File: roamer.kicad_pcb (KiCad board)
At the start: 4 copper layers, 39 x 99 mm, 97 parts, among them J1 Conn_Coaxial_Small, J2 JSTPH, J3 Conn_02x05_Odd_Even, J4 Conn_Coaxial_Small, J6 Conn_02x05_Odd_Even, J8 MEM2075-00-140-01-A, Q3 DMP2070UQ-7, SW1 KMR2, U1 2MB Flash, U2 AP2112K-3.3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

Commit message: Added mounting holes
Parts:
- removed JP2: SolderJumper_2_Open, Jumper:SolderJumper-2_P1.3mm_Open_TrianglePad1.0x1.5mm
- removed R29: 10K, Resistor_SMD:R_0603_1608Metric
- added C19: 1uF, Capacitor_SMD:C_0603_1608Metric, F.Cu at (243.8, 160.2)
- added H1: MountingHole, MountingHole:MountingHole_2.2mm_M2_DIN965_Pad, F.Cu at (220.5, 85.5)
- added H2: MountingHole, MountingHole:MountingHole_2.2mm_M2_DIN965_Pad, F.Cu at (220.2, 179.2)
- added H3: MountingHole, MountingHole:MountingHole_2.2mm_M2_DIN965_Pad, F.Cu at (253.8, 179.2)
- added H4: MountingHole, MountingHole:MountingHole_2.2mm_M2_DIN965_Pad, F.Cu at (253.5, 85.5)
- added H5: MountingHole, MountingHole:MountingHole_2.2mm_M2_DIN965_Pad, F.Cu at (220.5, 115.5)
- added R46: 0, Resistor_SMD:R_0603_1608Metric, F.Cu at (218.8, 134.5)
- added R47: 0, Resistor_SMD:R_0603_1608Metric, F.Cu at (218.8, 128.2)
- C10: value 10uF -> 1uF; footprint Inductor_SMD:L_0805_2012Metric -> Capacitor_SMD:C_0603_1608Metric
- moved TP8 4.32 mm to (253.6, 174.6)
- moved TP9 3.42 mm to (253.6, 170.5)
- moved J6 1.69 mm to (226.4, 177.4)
- moved R9 0.17 mm to (221.2, 167.5)
- moved C10 0.08 mm to (243.8, 152.2), turned to 90 degrees
- moved U1 0.08 mm to (240.0, 152.2)
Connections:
- C10 pad 1: +3V3 -> GND
- C10 pad 2: GND -> +3V3
- J2 pad 1: GND -> +BATT
- J2 pad 2: +BATT -> GND
- MCU1 pad 39: unconnected-(MCU1-PB16-Pad39) -> /Comms - LoRa 900/LORA_900_BUSY
- MCU1 pad 40: unconnected-(MCU1-PB17-Pad40) -> /Comms - LoRa 433/LORA_433_BUSY
- U4 pad 14: unconnected-(U4-DIO0-Pad14) -> Net-(U4-DIO0)
- U7 pad 5: Net-(JP2-B) -> unconnected-(U7-SDO-Pad5)
- U9 pad 14: unconnected-(U9-DIO0-Pad14) -> Net-(U9-DIO0)
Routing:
- net Net-(U4-DIO0): track 0.00 -> 36.2 mm, vias 0 -> 2
- net /Comms - LoRa 900/LORA_900_BUSY: track 0.00 -> 24.8 mm, vias 0 -> 2
- net /Comms - LoRa 433/LORA_433_BUSY: track 0.00 -> 17.6 mm, vias 0 -> 2
- net Net-(U9-DIO0): track 0.00 -> 14.6 mm, vias 0 -> 2
- net Net-(JP2-B): track 5.57 -> 0.00 mm, vias 1 -> 0
- net /Power - Management/IN-: track 30.8 -> 27.2 mm
- net Net-(U8-VS): track 2.81 -> 6.06 mm
- net +BATT: track 88.7 -> 85.8 mm
- net VBUS: track 60.7 -> 58.1 mm
- net /Bus - SPI/SPI.SCK: track 54.0 -> 56.6 mm
- net /Bus - SPI/SPI.MOSI: track 62.4 -> 60.7 mm
- net Net-(J3-Pin_10): track 35.9 -> 34.6 mm
- net Net-(D2-K): track 52.4 -> 51.1 mm
- net /Bus - SPI/SPI.MISO: track 69.4 -> 70.6 mm
- net +3V3: track 71.5 -> 72.7 mm, vias 16 -> 18
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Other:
- outline, holes or cut-outs redrawn

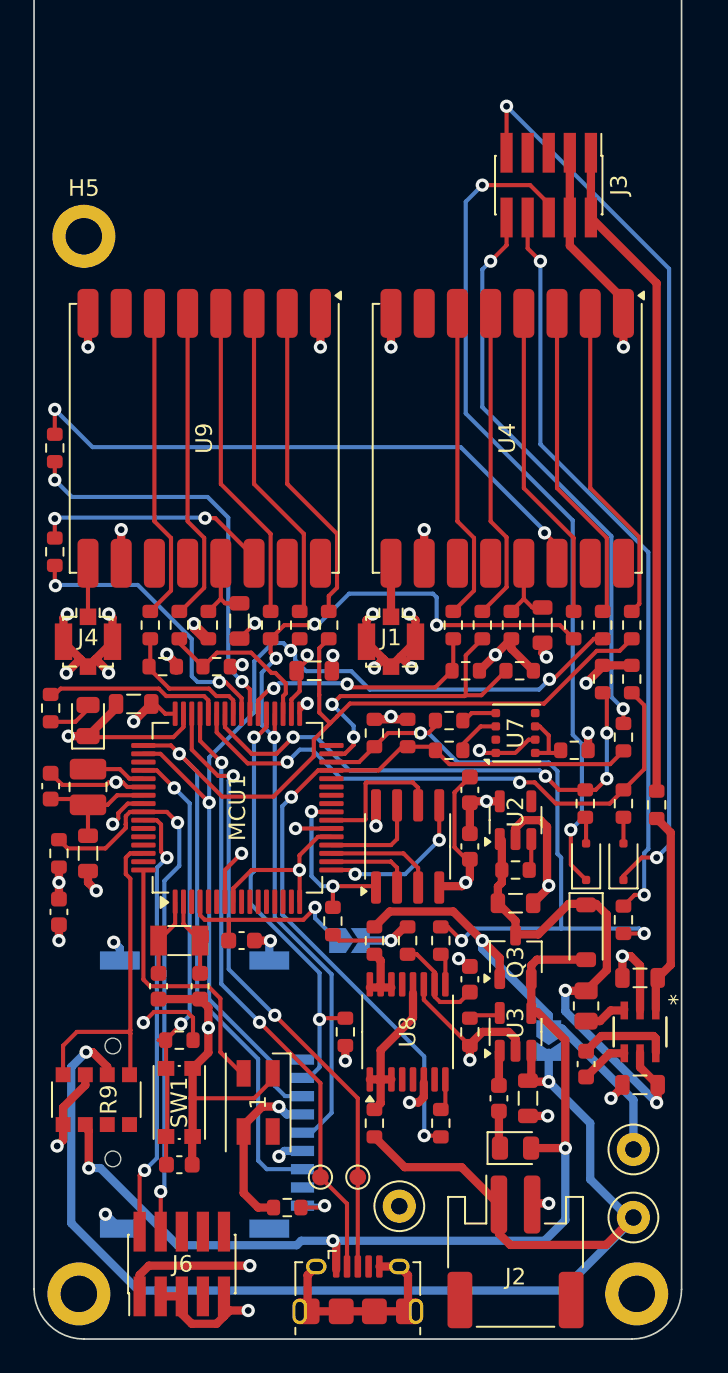
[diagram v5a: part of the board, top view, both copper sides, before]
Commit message: Cleaning up traces
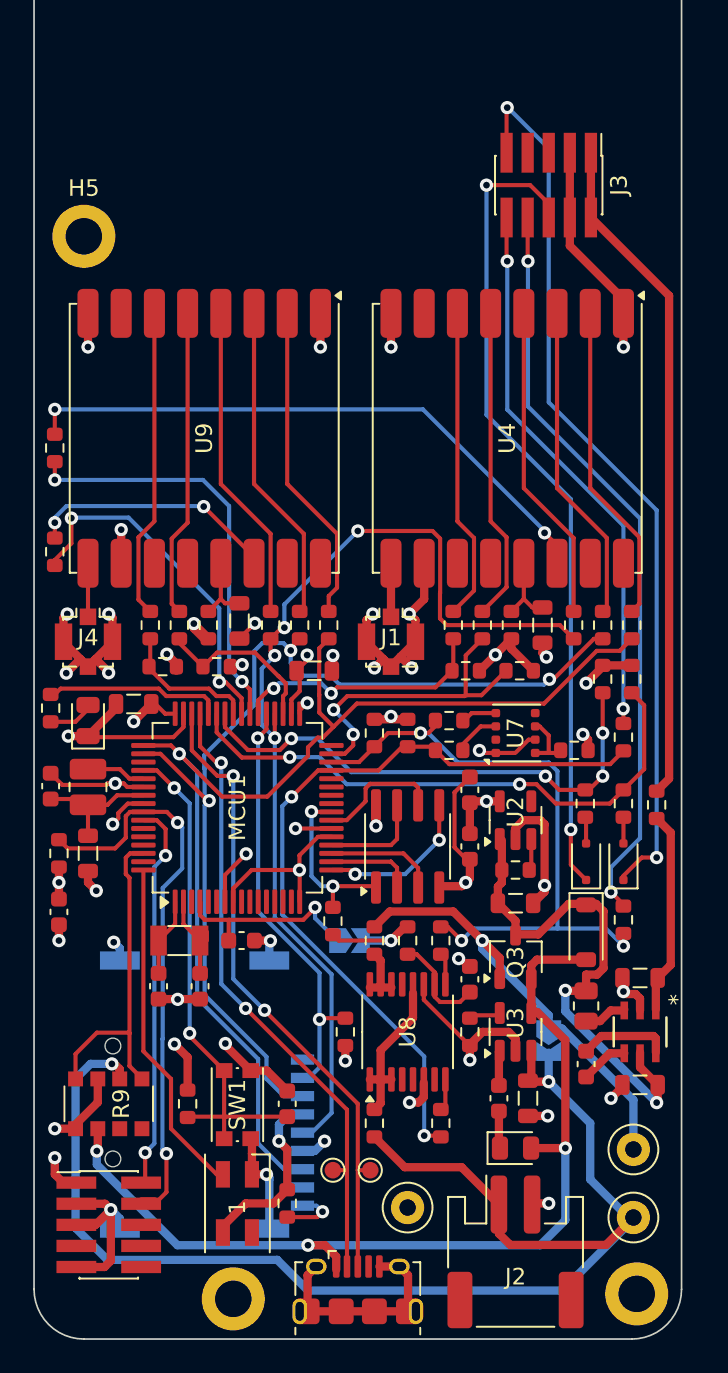
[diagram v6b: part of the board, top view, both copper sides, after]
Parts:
- removed J6: Conn_02x05_Odd_Even, Connector_PinHeader_1.27mm:PinHeader_2x05_P1.27mm_Vertical_SMD
- added J5: Conn_02x05_Odd_Even, Connector_PinHeader_1.27mm:PinHeader_2x05_P1.27mm_Vertical_SMD, F.Cu at (222.0, 175.0)
- moved H2 9.30 mm to (229.5, 179.5)
- moved C12 7.46 mm to (232.8, 167.8), turned to 90 degrees
- moved D1 6.21 mm to (229.8, 173.8)
- moved R1 3.86 mm to (226.8, 167.8), turned to 90 degrees
- moved SW1 3.50 mm to (229.8, 167.8)
- moved TP3 0.86 mm to (237.8, 171.8)
- moved TP4 0.86 mm to (235.5, 171.8)
- moved R9 0.79 mm to (222.0, 167.8)
- moved TP7 0.51 mm to (240.0, 174.0)
- moved R34 0.25 mm to (232.8, 173.8), turned to -90 degrees
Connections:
- net /MCU/SWCLK renamed /Interface - SWD/SWD.CLK
- MCU1 pad 58: /MCU/SWDIO -> /Interface - SWD/SWD.IO
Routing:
- net /MCU/SWDIO: track 26.5 -> 0.00 mm, vias 2 -> 0
- net /Interface - SWD/SWD.IO: track 0.00 -> 23.5 mm, vias 0 -> 2
- net +3V3: track 72.7 -> 66.0 mm
- net /Bus - SPI/SPI.SCK: track 56.6 -> 62.4 mm
- net /MCU/~{RESET}: track 26.5 -> 30.7 mm
- net /Comms - LoRa 433/LORA_433_BUSY: track 17.6 -> 21.6 mm
- net /MCU/D8_NEOPIX: track 16.9 -> 20.5 mm
- net GND: track 165.5 -> 162.1 mm
- net Net-(D2-K): track 51.1 -> 49.4 mm
- net /Bus - I2C/I2C.SCL: track 40.8 -> 39.3 mm
- net Net-(J3-Pin_10): track 34.6 -> 33.4 mm
- net Net-(D3-K): track 55.1 -> 54.2 mm
- net /MCU - Memory/QSPI.SCK: track 8.54 -> 7.66 mm
- net /Bus - SPI/SPI.MOSI: track 60.7 -> 61.6 mm
- net Net-(MCU1-PB01): track 21.0 -> 20.2 mm
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
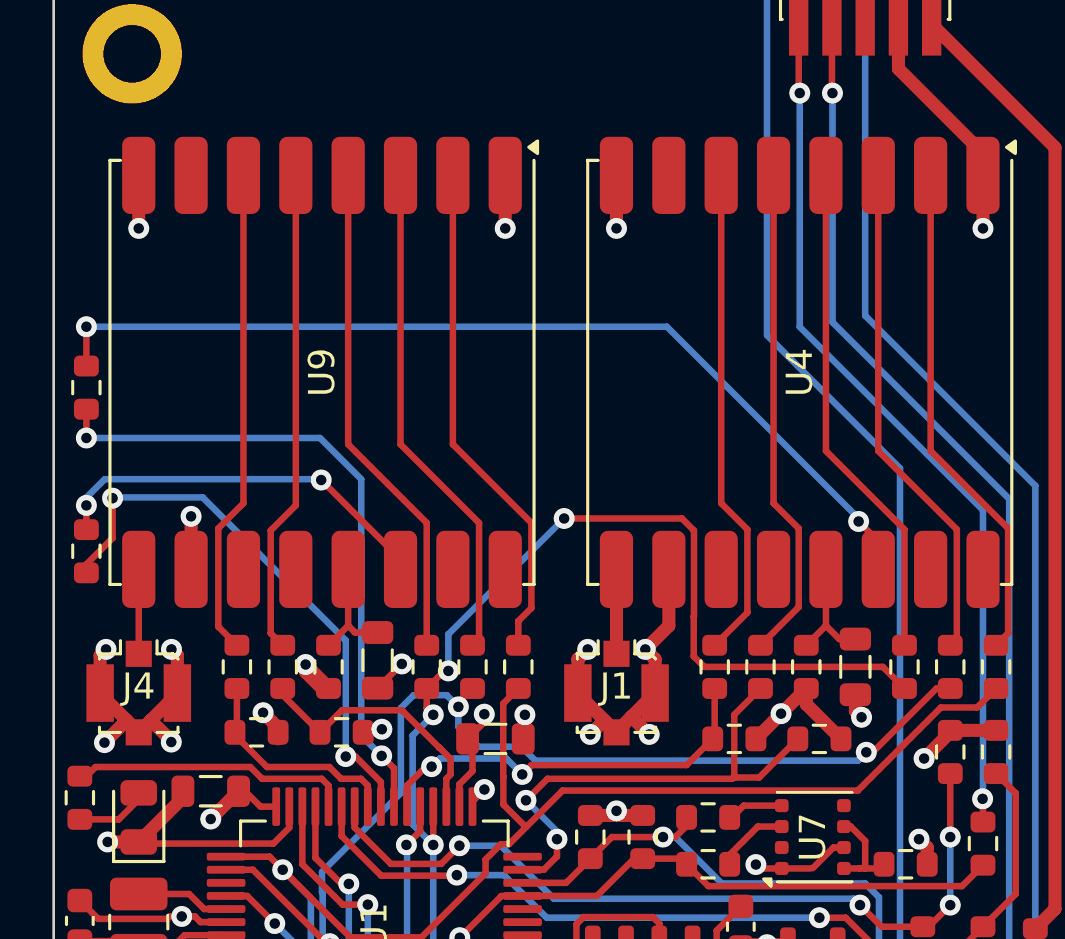
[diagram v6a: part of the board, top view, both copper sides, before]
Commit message: Adding via shielding for UFL connectors
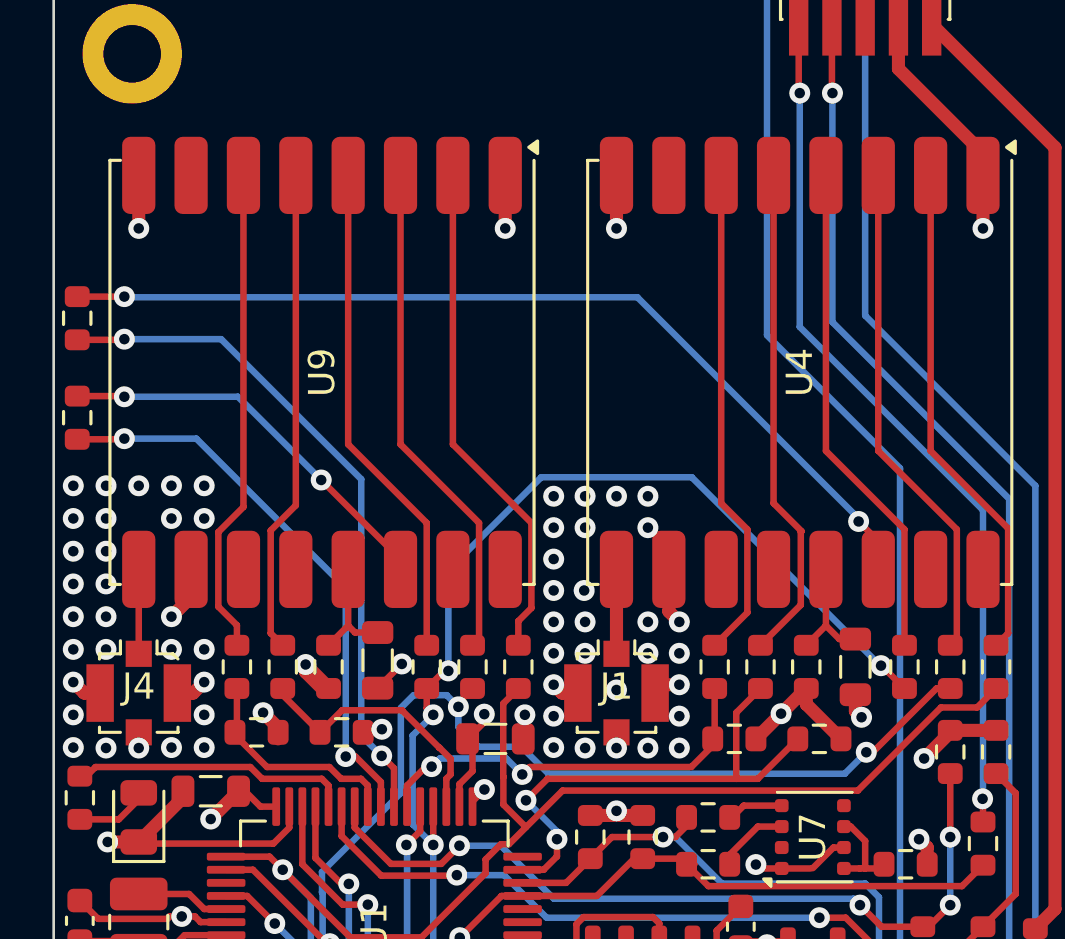
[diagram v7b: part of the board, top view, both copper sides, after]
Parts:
- moved R46 5.11 mm to (218.4, 129.4)
- moved R47 2.67 mm to (218.4, 125.6)
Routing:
- net GND: track 162.1 -> 147.2 mm, vias 42 -> 90
- net /Comms - LoRa 900/LORA_900_BUSY: track 25.3 -> 26.1 mm
- net Net-(U4-DIO0): track 36.2 -> 35.5 mm

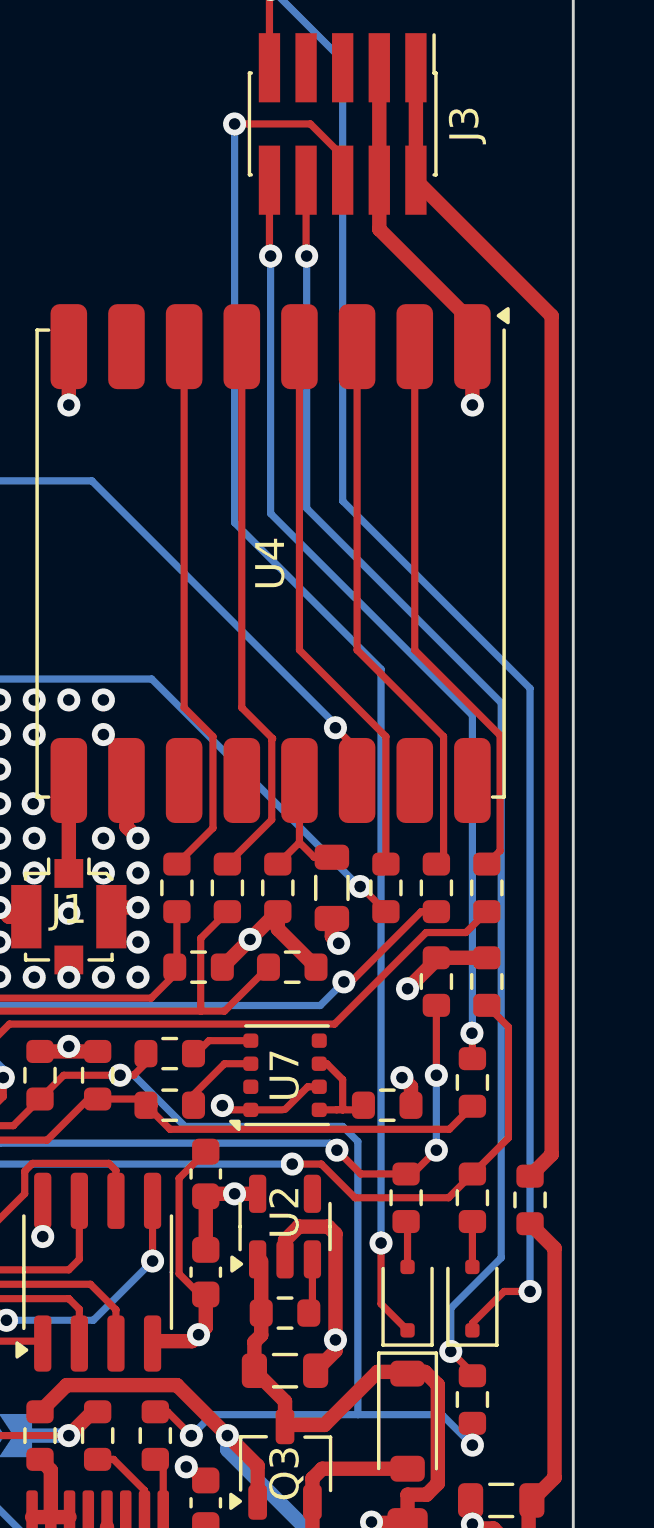
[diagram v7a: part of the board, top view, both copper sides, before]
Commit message: Added via shielding for 5v line
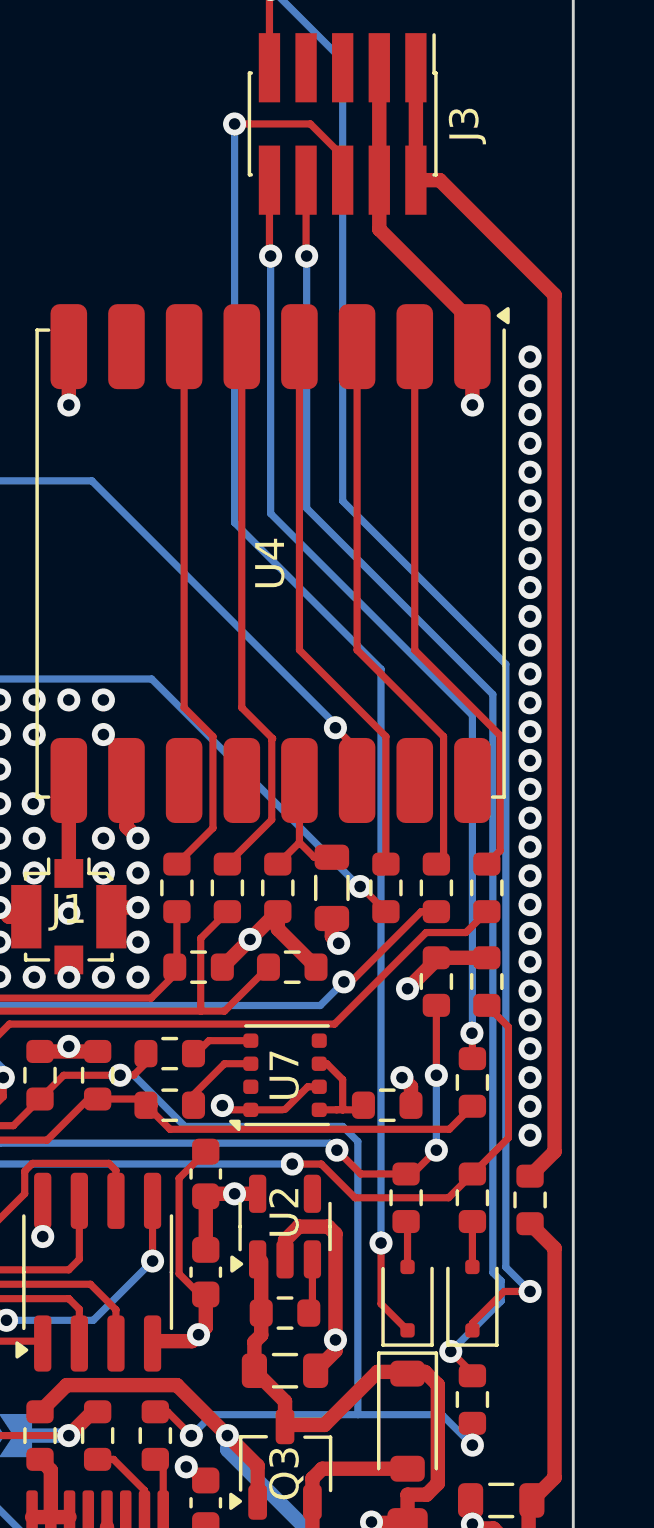
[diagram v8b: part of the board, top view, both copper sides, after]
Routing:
- net Net-(J3-Pin_1): track 40.7 -> 41.3 mm
- net GND: vias 90 -> 118
